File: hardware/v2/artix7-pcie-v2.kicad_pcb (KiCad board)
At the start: 4 copper layers, 60 x 51 mm, 191 parts, among them J1 Conn_02x20_Odd_Even, J10 USB_B_Micro, J2 Conn_02x20_Odd_Even, J3 JTAG_EN, J4 USB3_A, J5 USB3_A_AS_PCIE, J6 JTAG, J7 Conn_01x02, J8 SER, SW1 PROG, SW2 USER, U1 XC7A75T-FGG484, U2 W25Q64JVSSIM, U3 LP5907MFX, U4 5P49V6965A000NLGI, U5 TPS82130SILT, U6 TPS82150SILT, U7 TPS82150SILT, U8 TPS82130SILT, U9 TPS82150SILT, X1 25MHz/10pF

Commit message: v2 hardware: aug2020 pcb updates
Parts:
- removed C40, C41: 0.1uF/6.3V/X5R/PCIE, tom-passives:C_0402_1005Metric
- removed R11, R15, R19, R21, R33, R46, R47, R48, R49: 0R, tom-passives:R_0603_1608Metric_NoPaste
- removed R20, R50: 0R, tom-passives:R_0402_1005Metric_NoPaste
- removed R42, R44: DNP, tom-passives:R_0402_1005Metric_NoPaste
- removed R43, R45: 0R, tom-passives:R_0402_1005Metric
- added TP16: TestPoint, tom-mechanical:TestPoint_Pad_D1.5mm, B.Cu at (120.2, 84.3)
- added TP17: TestPoint, tom-mechanical:TestPoint_Pad_D1.5mm, B.Cu at (163.4, 85.5)
- added TP18: TestPoint, tom-mechanical:TestPoint_Pad_D1.5mm, B.Cu at (162.8, 87.9)
- added TP19: TestPoint, tom-mechanical:TestPoint_Pad_D1.5mm, B.Cu at (154.4, 82.8)
- added TP20: TestPoint, tom-mechanical:TestPoint_Pad_D1.5mm, B.Cu at (162.9, 82.9)
- C18, C23, C42, C44, C60, C67, C68, C78, C85, C86: footprint tom-passives:C_1206_3216Metric -> tom-passives:CP_EIA-3216-12_Kemet-S
- C3, C4: value 0.1uF/6.3V/X5R/PCIE -> 0.1uF/6.3V/X5R
- D3, D4: value SBR3U20SA-13‎ -> SBR3U20SA-13
- R1, R51: value 1K/5% -> 4.7k/5%
- R10, R9: value 10K/5% -> 4.7k/5%
- R12, R16, R22, R24, R36: value 100k/5% -> 100k/1%
- R18: value 213k/1% -> 215k/1%
- R26, R27: value 0R -> 270R/5%
- R30, R4: value 1k/5% -> 1k/1%
- SW1, SW2: footprint tom-mechanical:SW_Push_1P1T_NO_CK_KMR2 -> tom-mechanical:SW_Push_1P1T_NO_Vertical_Wuerth_434133025816
- U2: value W25Q64JVSSIM -> MX25L51245GZ2I-10G
- moved C4 32.4 mm to (159.0, 68.3), turned to 270 degrees
- moved C3 6.21 mm to (125.8, 68.2), turned to 270 degrees
- moved SW1 0.44 mm to (147.1, 104.0)
- moved SW2 0.34 mm to (147.1, 108.2)
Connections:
- C10 pad 1: /Power/VOUT_16 -> /VCCO_16
- C11 pad 2: /Power/VIN_1.8V -> VCC
- C12 pad 1: /Power/VIN_MGTAVTT -> +3V3
- C13 pad 2: /Power/VIN_34_35 -> VCC
- C14 pad 1: /Power/VOUT_MGTAVTT -> /MGTAVTT
- C3 pad 1: /OUT3_P -> Net-(C3-Pad1)
- C3 pad 2: /artix7-pcie-v2-serdes/MGT_REFCLK0_P -> GND
- C35 pad 1: /Power/VOUT_1.8V -> +1V8
- C37 pad 2: /Power/VIN_3.3V -> VCC
- C39 pad 1: /Power/VOUT_3.3V -> +3V3
- C4 pad 1: /OUT3_N -> Net-(C4-Pad1)
- C4 pad 2: /artix7-pcie-v2-serdes/MGT_REFCLK0_N -> GND
- C5 pad 2: /Power/VIN_1.0V -> VCC
- C7 pad 1: /Power/VOUT_1V -> +1V0
- C8 pad 2: /Power/VIN_16 -> VCC
- J4 pad 10: Net-(J4-Pad10) -> Net-(C3-Pad1)
- J5 pad 10: Net-(J5-Pad10) -> Net-(C4-Pad1)
- J5 pad 4: /artix7-pcie-v2-serdes/S2_GND -> /PCIE_PERST
- J5 pad 5: /artix7-pcie-v2-serdes/S2_RX_N -> /artix7-pcie-v2-serdes/S2_TX_N
- J5 pad 6: /artix7-pcie-v2-serdes/S2_RX_P -> /artix7-pcie-v2-serdes/S2_TX_P
- J5 pad 7: /artix7-pcie-v2-serdes/S2_DRAIN -> GND
- J5 pad 8: /artix7-pcie-v2-serdes/S2_TX_N -> /artix7-pcie-v2-serdes/S2_RX_N
- J5 pad 9: /artix7-pcie-v2-serdes/S2_TX_P -> /artix7-pcie-v2-serdes/S2_RX_P
- R12 pad 1: /Power/VOUT_1V -> +1V0
- R14 pad 2: /Power/VOUT_1V -> +1V0
- R16 pad 1: /Power/VOUT_16 -> /VCCO_16
- R18 pad 2: /Power/VOUT_16 -> /VCCO_16
- R22 pad 1: /Power/VOUT_1.8V -> +1V8
- R26 pad 1: Net-(J4-Pad10) -> Net-(C3-Pad1)
- R27 pad 1: Net-(J5-Pad10) -> Net-(C4-Pad1)
- R31 pad 2: /Power/VOUT_1.8V -> +1V8
- R36 pad 1: /Power/VOUT_3.3V -> +3V3
- R39 pad 2: /Power/VOUT_3.3V -> +3V3
- U1 pad A10: /artix7-pcie-v2-serdes/S2_RX_N -> /artix7-pcie-v2-serdes/S2_RX_P
- U1 pad B10: /artix7-pcie-v2-serdes/S2_RX_P -> /artix7-pcie-v2-serdes/S2_RX_N
- U3 pad 1: /Power/VIN_MGTAVTT -> +3V3
- U3 pad 5: /Power/VOUT_MGTAVTT -> /MGTAVTT
- U4 pad 13: /OUT3_N -> /artix7-pcie-v2-serdes/MGT_REFCLK0_N
- U4 pad 14: /OUT3_P -> /artix7-pcie-v2-serdes/MGT_REFCLK0_P
- U4 pad 16: /OUT2_N -> /CLKIN_N
- U4 pad 17: /OUT2_P -> /CLKIN_P
- U5 pad 1: /Power/VIN_1.0V -> VCC
- U5 pad 2: /Power/VIN_1.0V -> VCC
- U5 pad 4: /Power/VOUT_1V -> +1V0
- U5 pad 5: /Power/VOUT_1V -> +1V0
- U6 pad 2: /Power/VIN_16 -> VCC
- U6 pad 4: /Power/VOUT_16 -> /VCCO_16
- U6 pad 5: /Power/VOUT_16 -> /VCCO_16
- U7 pad 2: /Power/VIN_1.8V -> VCC
- U7 pad 4: /Power/VOUT_1.8V -> +1V8
- U7 pad 5: /Power/VOUT_1.8V -> +1V8
- U8 pad 2: /Power/VIN_34_35 -> VCC
- U9 pad 2: /Power/VIN_3.3V -> VCC
- U9 pad 4: /Power/VOUT_3.3V -> +3V3
- U9 pad 5: /Power/VOUT_3.3V -> +3V3
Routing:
- net /artix7-pcie-v2-serdes/S2_GND: track 25.7 -> 0.00 mm, vias 3 -> 0
- net VCC: track 106.0 -> 130.3 mm
- net +1V8: track 33.6 -> 56.5 mm
- net +3V3: track 256.5 -> 279.2 mm
- net Net-(C4-Pad1): track 0.00 -> 19.8 mm
- net /PCIE_PERST: track 33.6 -> 52.5 mm, vias 3 -> 4
- net Net-(J5-Pad10): track 18.6 -> 0.00 mm
- net +1V0: track 53.6 -> 71.8 mm
- net Net-(C3-Pad1): track 0.00 -> 18.1 mm
- net /Power/VOUT_3.3V: track 17.9 -> 0.00 mm
- net /Power/VOUT_1.8V: track 17.7 -> 0.00 mm
- net Net-(J4-Pad10): track 17.3 -> 0.00 mm
- net /VCCO_16: track 90.5 -> 107.6 mm
- net /Power/VOUT_16: track 17.0 -> 0.00 mm
- net /Power/VOUT_1V: track 17.0 -> 0.00 mm
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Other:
- board text added: "6"
- board text added: "Aug2020"
- board text added: "G"
- board text added: "N|P"
- board text added: "PCIe"
- board text added: "P|N"
- board text added: "USB 3.0"
- board text added: "arctic serdes"
- board text removed: "Apr2020"
- board text removed: "red yeti"

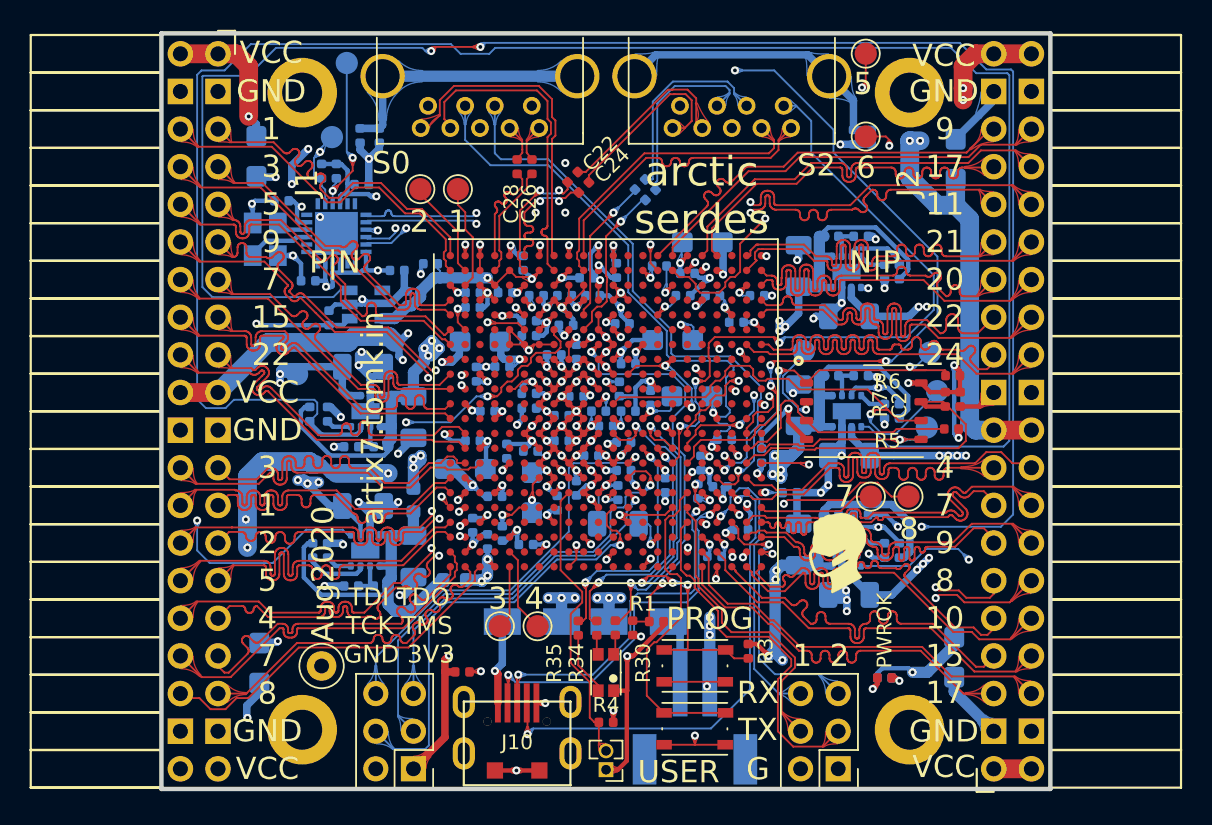
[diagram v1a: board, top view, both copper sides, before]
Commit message: v2 hardware: Aug2020/rc2 version - flip tx/rx pairs on s2 - add lcsc part numbers
rc2 errata schematic
- change serial port connector to add +3.3V ? (8-pin)(NO)
- add test points for flash pre-programming
- smaller package on input direction diodes (NO)
- bom dupe errors
- remove all p/s 0R bringup parts
- optimise bom (use 1.5k for led, 10k/4.7k for i2c pullups)
- done led is bright (change to 4.7k)
- improve shield grounding with RC
- check actual values of RGB resistors
- remove caps from clock inputs

rc2 errata pcb
- no gnd marking on serial port connector pins
- change serial port connector to add +3.3V ? (8-pin) (NO)
- no test points for flash pre-programming
- missing caps on xtal? (No but select xtal carefully)
- Cfg sel pins on clock chip?
- No silk on test points
- No +/- pair numbering on silk
- vcc test points for clk pre-programming? (or use bootloader)
- random silk circle under S2
- smaller package on input direction diodes (NO)
- no polarity on 100uF tantalum
- some via in or close to pads
- wrong button package (change from feather to chinese)
- gnd/vcc labels swapped at high end of J2
- clock chip OUT0_SEL_I2CB needs to be tied high after programming
- check teardrops
- power diode footprint marking reverse
- LEDs use cap footprint
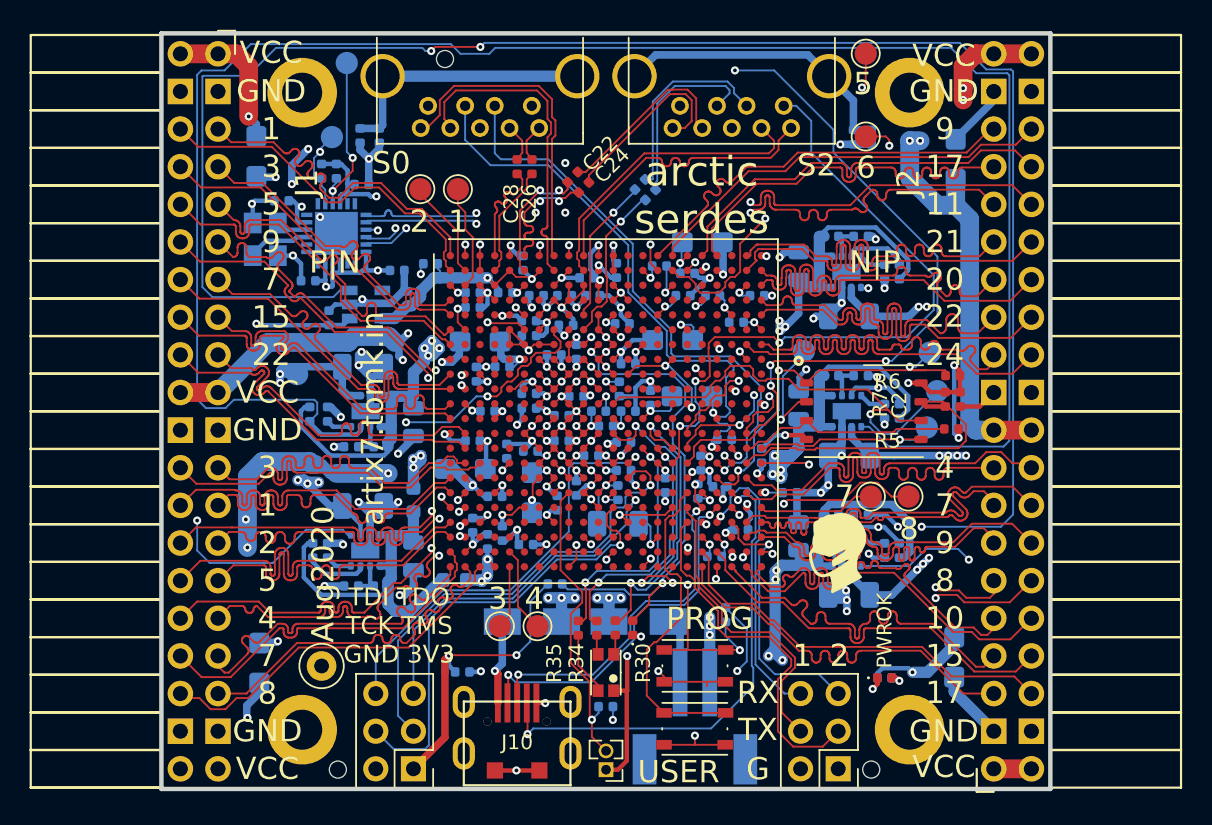
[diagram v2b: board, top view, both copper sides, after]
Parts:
- added H2: mech-only-no-pins, tom-mechanical:JLCPCB_ASSEMBLY_TOOL_HOLE, F.Cu at (123.0, 111.0)
- added H3: mech-only-no-pins, tom-mechanical:JLCPCB_ASSEMBLY_TOOL_HOLE, F.Cu at (130.2, 63.0)
- added H4: mech-only-no-pins, tom-mechanical:JLCPCB_ASSEMBLY_TOOL_HOLE, F.Cu at (130.9, 111.0)
- C10, C35, C36, C39, C7: footprint tom-passives:C_1206_3216Metric -> tom-passives:C_0805_2012Metric
- C17, R1, R3, R4: moved to B.Cu
- D1, D5: footprint tom-passives:C_0402_1005Metric -> tom-opto:LED_0402_1005Metric
- U3: value LP5907MFX -> LP5907MFX-1.2
- moved R1 7.30 mm to (137.7, 98.5), turned to 0 degrees
- moved R3 2.90 mm to (149.2, 100.5)
- moved R4 1.06 mm to (141.1, 106.8)
- moved C39 0.56 mm to (154.1, 95.2)
- moved C7 0.34 mm to (128.1, 87.5)
- turned D3 to 0 degrees
- turned D4 to 180 degrees
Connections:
- D3 pad 1: /VCC_IN -> VCC
- D3 pad 2: VCC -> /VCC_IN
- D4 pad 1: /VBUS -> VCC
- D4 pad 2: VCC -> /VBUS
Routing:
- net +3V3: track 279.2 -> 290.8 mm, vias 25 -> 27
- net /DONE: track 27.1 -> 33.9 mm
- net /CFG_FLASH_WP_D2: track 16.8 -> 14.5 mm
- net /PROG_B: track 29.6 -> 31.4 mm, vias 4 -> 5
- net /CFG_FLASH_MISO_D1: track 13.1 -> 14.8 mm
- net /M2: track 19.8 -> 20.6 mm, vias 0 -> 1
- net +1V0: track 71.8 -> 72.6 mm
- net /artix7-pcie-v2-bank14/IO_L14_14_N: track 25.5 -> 24.8 mm
- net /artix7-pcie-v2-bank14/IO_L14_14_P: track 25.6 -> 24.9 mm

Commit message: v2 hardware : fix isues found by jlcpcb - change 0603 parts to add paste as they are now loaded - fix solder paste/mask issues with TPS power modules
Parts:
- R40, R41: footprint tom-passives:R_0603_1608Metric_NoPaste -> tom-passives:R_0603_1608Metric

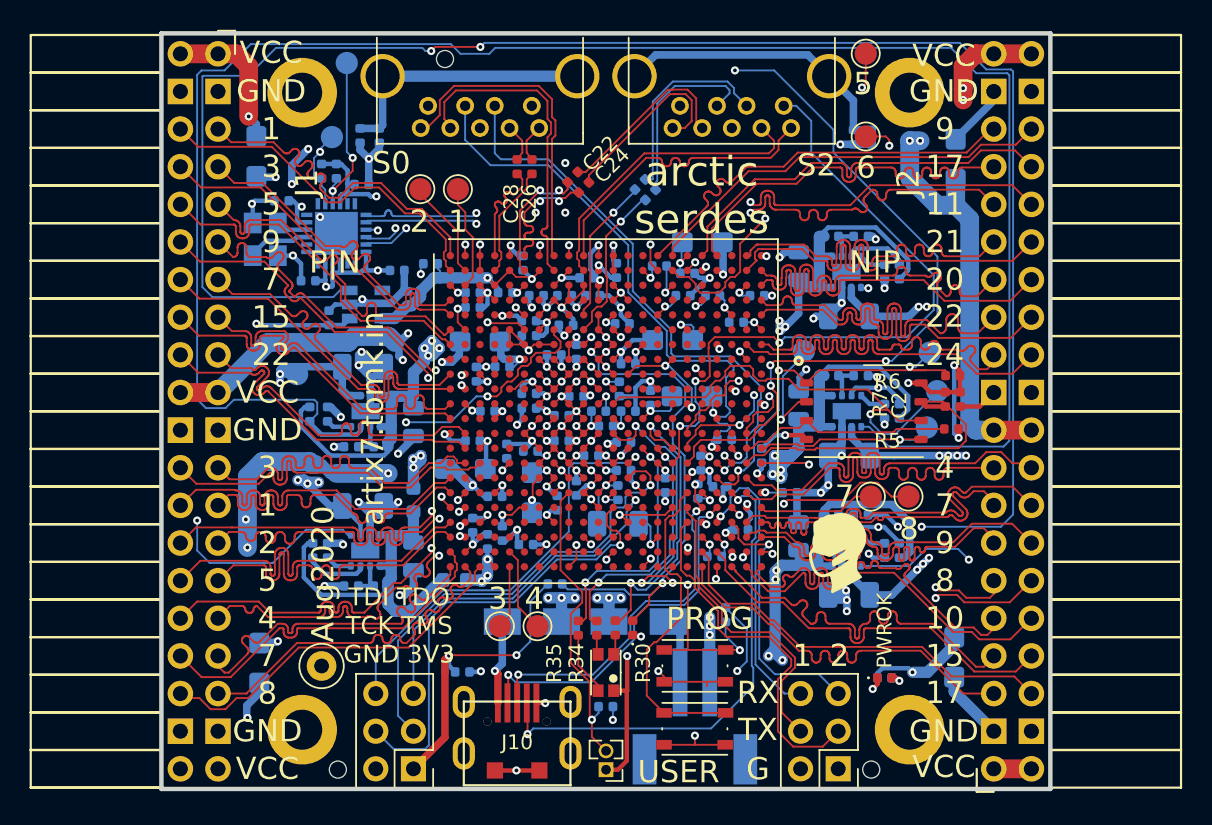
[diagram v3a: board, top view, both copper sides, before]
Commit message: JLC power supplies almost routed VCCBRAM to go Need to - check BOM - add power good leds - fix vccbram inc caps - fix 100uF part number - update silk
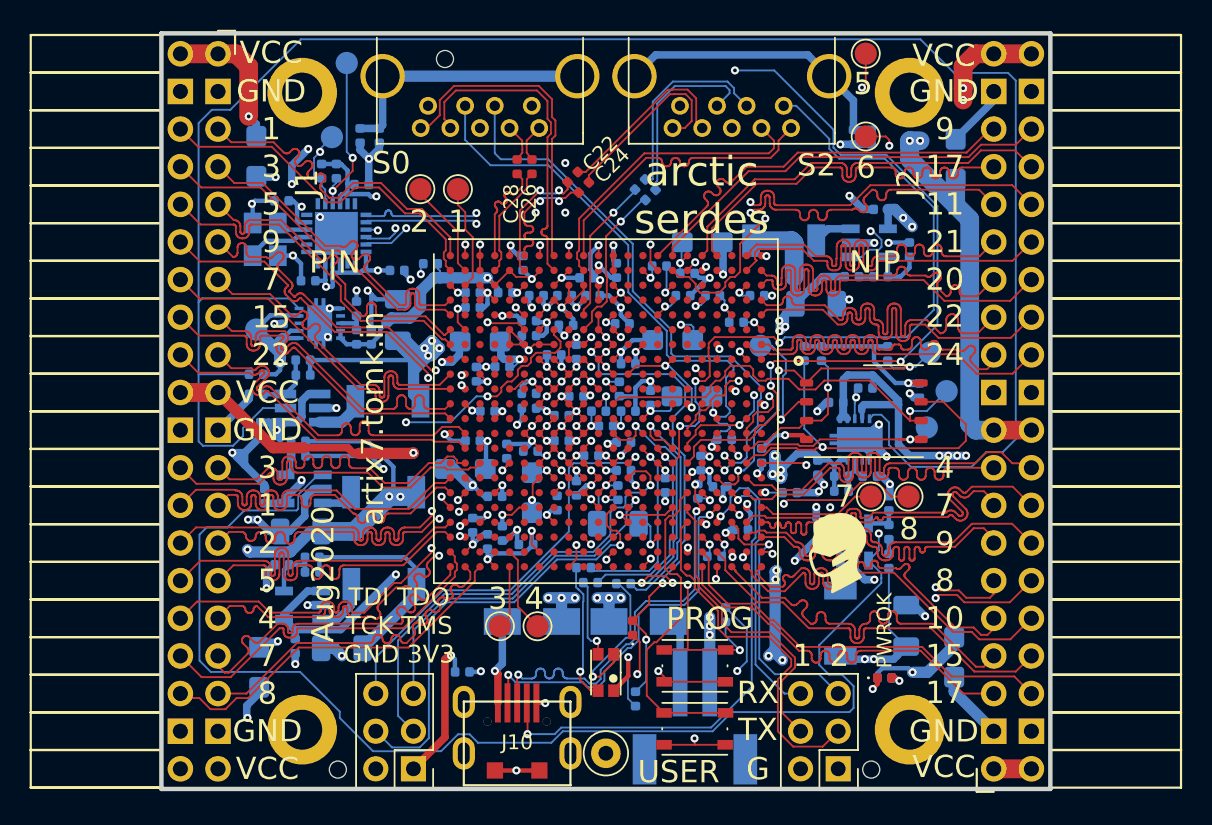
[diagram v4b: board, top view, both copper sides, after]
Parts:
- removed C37: 10uF/25V/X7R, tom-passives:C_1206_3216Metric
- removed C38: 3.3nF/25V, tom-passives:C_0402_1005Metric
- removed C39: 22uF/6.3V/X7S, tom-passives:C_0805_2012Metric
- removed J3: JTAG_EN, tom-connectors:PinHeader_1x02_P1.27mm_Vertical
- removed R4: 1k/1%, tom-passives:R_0402_1005Metric
- removed R40, R41: 0R, tom-passives:R_0603_1608Metric
- added L1: 2.2uH/4.5A, tom-passives:L_MWSA0518S, B.Cu at (156.9, 101.1)
- added L2: 2.2uH/4.5A, tom-passives:L_MWSA0518S, B.Cu at (126.4, 86.1)
- added L3: 2.2uH/4.5A, tom-passives:L_MWSA0518S, B.Cu at (126.1, 92.3)
- added L4: 2.2uH/4.5A, tom-passives:L_MWSA0518S, B.Cu at (153.1, 75.3)
- added L5: 2.2uH/4.5A, tom-passives:L_MWSA0518S, B.Cu at (126.1, 98.5)
- added R11: 100k/1%, tom-passives:R_0402_1005Metric, B.Cu at (117.5, 84.3)
- added R15: 150k/1%, tom-passives:R_0402_1005Metric, B.Cu at (160.2, 96.9)
- added R19: 200k/1%, tom-passives:R_0402_1005Metric, B.Cu at (120.3, 88.8)
- added R20: 100k/1%, tom-passives:R_0402_1005Metric, B.Cu at (161.6, 75.9)
- added R21: 100k/1%, tom-passives:R_0402_1005Metric, B.Cu at (119.2, 97.2)
- added R33: 100k/1%, tom-passives:R_0402_1005Metric, B.Cu at (158.6, 85.2)
- added U10: TPS74701DRCR, artix7-pcie-v2:16624-01YE, B.Cu at (157.9, 88.7)
- C10, C35, C36: value 22uF/6.3V/X7S -> 4.7uF/10V/X5R; footprint tom-passives:C_0805_2012Metric -> tom-passives:C_0402_1005Metric
- C11, C5, C8: value 10uF/25V/X7R -> 4.7uF/10V/X5R; footprint tom-passives:C_1206_3216Metric -> tom-passives:C_0402_1005Metric
- C12, C14: value 1uF/6.3V/X5R -> 47uF/10V/X7R; footprint tom-passives:C_0402_1005Metric -> tom-passives:C_1206_3216Metric
- C15, C16, C6: value 3.3nF/25V -> 4.7uF/10V/X5R
- C2, R30, R34, R35, R5, R6, R7: moved to B.Cu
- C7: value 22uF/6.3V/X7S -> 10uF/25V/X7R; footprint tom-passives:C_0805_2012Metric -> tom-passives:C_1206_3216Metric
- C9: value 3.3nF/25V -> 47uF/10V/X7R; footprint tom-passives:C_0402_1005Metric -> tom-passives:C_1206_3216Metric
- R13, R22: value 100k/1% -> 300k/1%
- R14: value 24.9k/1% -> 100k/1%
- R16, R23, R36: value 100k/1% -> 200k/1%
- R18: value 215k/1% -> 100k/1%
- R25: value 100k/1% -> 18k/1%
- R31: value 124k/1% -> 150k/1%
- R32: value 124k/1% -> 100k/1%
- R39: value 316k/1% -> 330k/1%
- U3: value LP5907MFX-1.2 -> TLV62569DBVR; footprint tom-semiconductors:SOT-23-5 -> artix7-pcie-v2:SOT95P280X145-5N
- U5: value TPS82130SILT -> TLV62569PDDCR; footprint tom-modules:TPS82130SILT -> artix7-pcie-v2:SOT95P280X110-6N
- U6, U7: value TPS82150SILT -> TLV62569DBVR; footprint tom-modules:TPS82130SILT -> artix7-pcie-v2:SOT95P280X145-5N
- U8: value TPS82130SILT -> TLV62569DBVR; footprint tom-modules:TPS82130SILT -> artix7-pcie-v2:SOT95P280X145-5N
- U9: value TPS82150SILT -> TPS74701DRCR; footprint tom-modules:TPS82130SILT -> artix7-pcie-v2:16624-01YE
- moved C8 41.3 mm to (118.1, 92.5), turned to 270 degrees
- moved C15 40.9 mm to (119.3, 81.4), turned to 270 degrees
- moved R16 40.7 mm to (120.6, 83.4), turned to 180 degrees
- moved R25 39.7 mm to (157.7, 77.7), turned to 0 degrees
- moved R12 39.6 mm to (160.2, 93.0), turned to 90 degrees
- moved C11 39.5 mm to (120.1, 102.7), turned to 90 degrees
- moved U6 39.4 mm to (120.7, 92.1), turned to 180 degrees
- moved R23 39.3 mm to (121.3, 97.7), turned to 180 degrees
- moved R18 38.9 mm to (120.3, 89.8), turned to 0 degrees
- moved R17 38.8 mm to (120.7, 84.4), turned to 180 degrees
- moved U9 38.7 mm to (121.8, 80.9), turned to 0 degrees
- moved R13 36.7 mm to (160.2, 95.0), turned to 90 degrees
- moved U3 36.7 mm to (157.9, 95.6), turned to 90 degrees
- moved C7 36.0 mm to (161.4, 101.3)
- moved C16 35.8 mm to (156.6, 86.2), turned to 0 degrees
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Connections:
- C10 pad 1: /VCCO_16 -> GND
- C10 pad 2: GND -> VCC
- C12 pad 1: +3V3 -> GND
- C12 pad 2: GND -> /VCCO_34
- C13 pad 2: VCC -> /VCCO_16
- C14 pad 1: /MGTAVTT -> GND
- C14 pad 2: GND -> /Power/VCCBRAM
- C15 pad 2: /Power/SSTR_1.8V -> VCC
- C16 pad 2: /Power/SSTR_34_35 -> VCC
- C23 pad 1: /VCCO_35 -> /VCCO_34
- C35 pad 1: +1V8 -> GND
- C35 pad 2: GND -> /MGTAVTT
- C36 pad 1: /Power/VCCO_34_35 -> GND
- C36 pad 2: GND -> +1V8
- C43 pad 1: +1V0 -> /Power/VCCBRAM
- C49 pad 1: +1V0 -> /Power/VCCBRAM
- C6 pad 2: /Power/SSTR_1.0V -> VCC
- C69 pad 1: +1V0 -> /Power/VCCBRAM
- C7 pad 1: +1V0 -> GND
- C7 pad 2: GND -> +3V3
- C86 pad 1: /VCCO_35 -> /VCCO_34
- C88 pad 1: /VCCO_35 -> /VCCO_34
- C9 pad 2: /Power/SSTR_16 -> +1V0
- C90 pad 1: /VCCO_35 -> /VCCO_34
- C92 pad 1: /VCCO_35 -> /VCCO_34
- C94 pad 1: /VCCO_35 -> /VCCO_34
- C96 pad 1: /VCCO_35 -> /VCCO_34
- C98 pad 1: /VCCO_35 -> /VCCO_34
- J1 pad 1: /VCCO_35 -> /VCCO_34
- J1 pad 19: /VCCO_35 -> /VCCO_34
- J1 pad 2: /VCCO_35 -> /VCCO_34
- J1 pad 20: /VCCO_35 -> /VCCO_34
- R12 pad 1: +1V0 -> /Power/FB_3.3V
- R12 pad 2: /Power/PG_1.0V -> GND
- R13 pad 1: /Power/FB_1.0V -> Net-(R13-Pad1)
- R13 pad 2: GND -> /Power/FB_3.3V
- R14 pad 2: +1V0 -> GND
- R16 pad 1: /VCCO_16 -> +1V0
- R16 pad 2: /Power/PG_16 -> /Power/FB_1.0V
- R17 pad 1: /Power/FB_16 -> +1V0
- R17 pad 2: GND -> /Power/FB_1.0V
- R18 pad 1: /Power/FB_16 -> /Power/FB_VCCO_34_35
- R18 pad 2: /VCCO_16 -> GND
- R22 pad 1: +1V8 -> Net-(R22-Pad1)
- R22 pad 2: /Power/PG_1.8V -> /Power/FB_VCCO_16
- R23 pad 1: /Power/FB_1.8V -> /Power/VCCBRAM
- R23 pad 2: GND -> /Power/FB_VCCBRAM
- R24 pad 1: /Power/VCCO_34_35 -> /Power/VCCBRAM
- R24 pad 2: /Power/PG_34_35 -> /Power/FB_VCCBRAM
- R25 pad 1: /Power/FB_34_35 -> /VCCO_16
- R25 pad 2: GND -> Net-(R22-Pad1)
- R31 pad 1: /Power/FB_1.8V -> /MGTAVTT
- R31 pad 2: +1V8 -> /Power/FB_MGTAVTT
- R32 pad 1: /Power/FB_34_35 -> /Power/FB_MGTAVTT
- R32 pad 2: /Power/VCCO_34_35 -> GND
- R36 pad 1: +3V3 -> +1V8
- R36 pad 2: /Power/PG_3.3V -> /Power/FB_1.8V
- R38 pad 1: /Power/FB_3.3V -> /Power/FB_1.8V
- R39 pad 1: /Power/FB_3.3V -> +1V8
- R39 pad 2: +3V3 -> /Power/FB_1.8V
- U1 pad C1: /VCCO_35 -> /VCCO_34
- U1 pad F2: /VCCO_35 -> /VCCO_34
- U1 pad H6: /VCCO_35 -> /VCCO_34
- U1 pad J11: +1V0 -> /Power/VCCBRAM
- U1 pad J3: /VCCO_35 -> /VCCO_34
- U1 pad L11: +1V0 -> /Power/VCCBRAM
- U1 pad M4: /VCCO_35 -> /VCCO_34
- U1 pad N1: /VCCO_35 -> /VCCO_34
- U1 pad N11: +1V0 -> /Power/VCCBRAM
- U1 pad U9: /M2 -> GND
- U3 pad 1: +3V3 -> /Power/PG_1.8V
- U3 pad 3: /Power/PG_3.3V -> /Power/SW_3.3V
- U3 pad 4: Net-(U3-Pad4) -> VCC
- U3 pad 5: /MGTAVTT -> /Power/FB_3.3V
- U5 pad 2: VCC -> GND
- U5 pad 3: GND -> /Power/SW_1.0V
- U5 pad 4: +1V0 -> VCC
- U5 pad 5: +1V0 -> /Power/PG_1.0V
- U6 pad 2: VCC -> GND
- U6 pad 3: GND -> /Power/SW_VCCO_34_35
- U6 pad 4: /VCCO_16 -> VCC
- U6 pad 5: /VCCO_16 -> /Power/FB_VCCO_34_35
- U7 pad 1: /Power/PG_1.0V -> /Power/PG_1.8V
- U7 pad 2: VCC -> GND
- U7 pad 3: GND -> /Power/SW_VCCO_16
- U7 pad 4: +1V8 -> VCC
- U7 pad 5: +1V8 -> /Power/FB_VCCO_16
- U8 pad 1: /Power/PG_1.8V -> VCC
- U8 pad 2: VCC -> GND
- U8 pad 3: GND -> /Power/SW_VCCBRAM
- U8 pad 4: /Power/VCCO_34_35 -> VCC
- U8 pad 5: /Power/VCCO_34_35 -> /Power/FB_VCCBRAM
- U9 pad 1: /Power/PG_1.8V -> VCC
- U9 pad 3: GND -> Net-(U9-Pad3)
- U9 pad 4: +3V3 -> VCC
- U9 pad 5: +3V3 -> /Power/PG_1.0V
- U9 pad 6: /Power/FB_3.3V -> GND
- U9 pad 7: /Power/PG_3.3V -> Net-(U9-Pad7)
- U9 pad 8: /Power/SSTR_3.3V -> /Power/FB_MGTAVTT
- U9 pad 9: GND -> /MGTAVTT
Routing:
- net /Power/PG_3.3V: track 125.1 -> 0.00 mm, vias 4 -> 0
- net /VCCO_35: track 96.9 -> 0.00 mm, vias 12 -> 0
- net /VCCO_34: track 76.9 -> 171.4 mm, vias 12 -> 18
- net /Power/PG_1.8V: track 165.3 -> 119.7 mm, vias 4 -> 3
- net VCC: track 130.3 -> 171.4 mm, vias 20 -> 18
- net +3V3: track 290.8 -> 261.4 mm, vias 27 -> 25
- net /Power/VCCO_34_35: track 23.5 -> 0.00 mm
- net /M2: track 20.6 -> 0.00 mm, vias 1 -> 0
- net /Power/VCCBRAM: track 0.00 -> 16.5 mm, vias 0 -> 1
- net +1V8: track 56.5 -> 40.5 mm
- net +1V0: track 72.6 -> 62.8 mm, vias 25 -> 23
- net Net-(D2-Pad1): track 1.35 -> 10.4 mm, vias 0 -> 1
- net /Power/PG_1.0V: track 128.6 -> 135.4 mm
- net /artix7-pcie-v2-bank14/IO_L8_14_N: track 27.4 -> 21.4 mm
- net Net-(D2-Pad4): track 4.30 -> 9.41 mm, vias 0 -> 1
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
